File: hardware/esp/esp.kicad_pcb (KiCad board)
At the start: 2 copper layers, 100 x 80 mm, 89 parts, among them J1 Conn_01x02, J2 USB_C_Receptacle_USB2.0_16P, J3 USB_C_Receptacle_USB2.0_16P, J4 Conn_01x02, J5 Conn_Coaxial, J6 Conn_01x09_Pin, J7 Conn_01x06_Pin, J8 Conn_01x09_Pin, SW1 RESET, SW2 BOOT, U1 AMS1117-3.3, U2 CP2102N-Axx-xQFN20, U3 ESP32-S3-WROOM-1, U4 VL53L0X, U5 NRF24L01, U6 BME280, Y1 16MHz

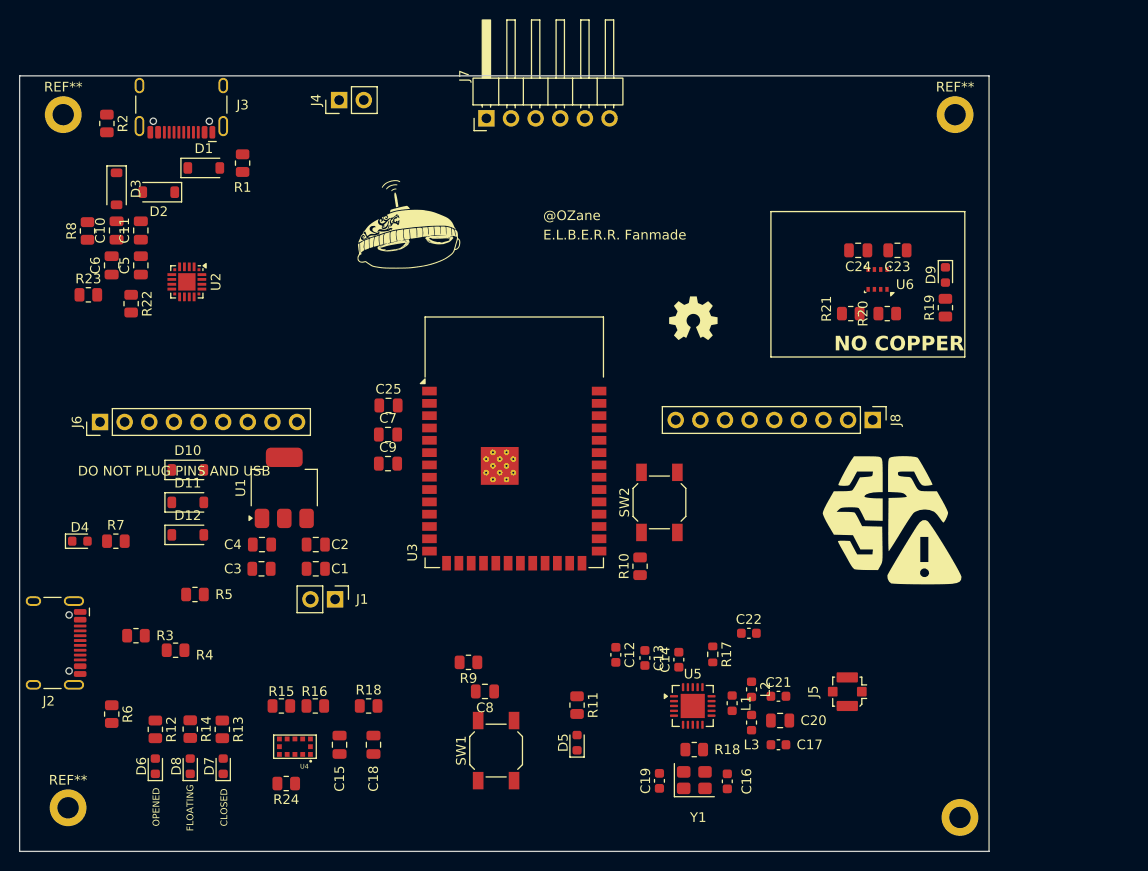
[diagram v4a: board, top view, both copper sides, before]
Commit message: Updating schematic, BOM, and component placement on PCB
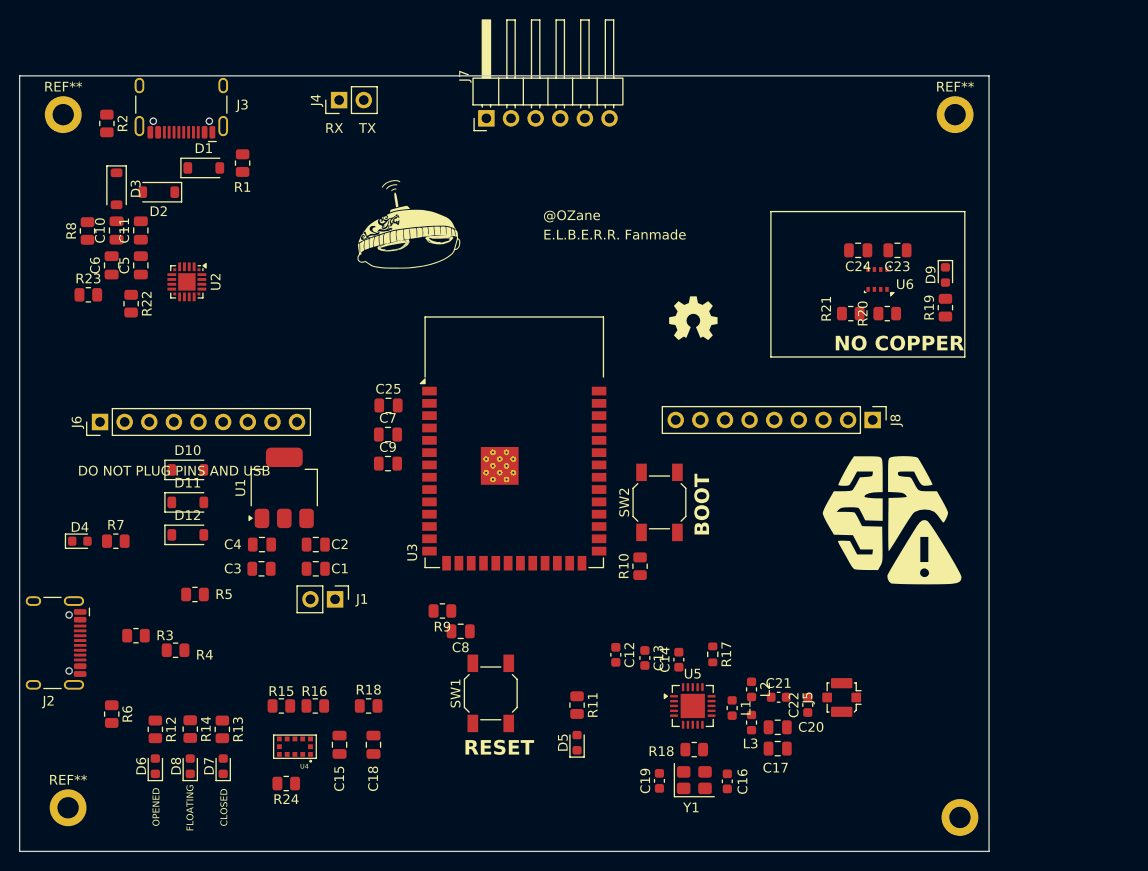
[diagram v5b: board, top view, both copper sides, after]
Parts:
- C17: footprint Capacitor_SMD:C_0603_1608Metric -> Capacitor_SMD:C_0805_2012Metric
- moved C22 9.57 mm to (166.3, 134.9), turned to 90 degrees
- moved C8 6.69 mm to (130.5, 127.3)
- moved R9 5.94 mm to (128.6, 125.2)
- moved SW1 5.93 mm to (133.6, 133.7)
- moved J5 0.83 mm to (169.8, 134.1)
- moved C20 0.74 mm to (163.2, 137.2)
- moved L1 0.50 mm to (158.5, 135.2)
- moved C17 0.41 mm to (163.2, 139.4)
- moved C21 0.10 mm to (163.3, 134.1)
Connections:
- C24 pad 1: +3V3 -> GND
- C24 pad 2: GND -> +3V3
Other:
- board text added: "BOOT"
- board text added: "RESET"

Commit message: Updating PCB
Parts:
- removed the R18 at (121.0, 135.0)
- moved D10 20.8 mm to (98.0, 131.0), turned to -90 degrees
- moved D11 12.8 mm to (98.0, 126.0), turned to 90 degrees
- moved D12 9.94 mm to (94.0, 122.8), turned to 90 degrees
- moved C12 8.70 mm to (155.2, 129.5), turned to 180 degrees
- moved C13 5.82 mm to (155.2, 131.2), turned to 180 degrees
- moved R4 5.49 mm to (106.6, 129.2)
- moved R3 5.49 mm to (102.5, 127.7)
- moved C6 3.01 mm to (97.5, 89.6)
- moved C10 2.50 mm to (97.5, 85.9)
- moved C11 2.50 mm to (95.0, 85.9)
- moved C5 2.50 mm to (95.0, 89.6)
- moved R17 1.49 mm to (157.8, 130.4)
- moved L2 1.04 mm to (161.0, 134.2), turned to 0 degrees
- moved C21 1.00 mm to (164.3, 134.2)
- moved C22 1.00 mm to (167.3, 135.0)
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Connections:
- U5 pad 21: (no net) -> GND
- U5 pad 3: SPI_SCK -> SCK
- U5 pad 4: SPI_MOSI -> MOSI
- U5 pad 5: SPI_MISO -> MISO
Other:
- board text removed: "NO COPPER"

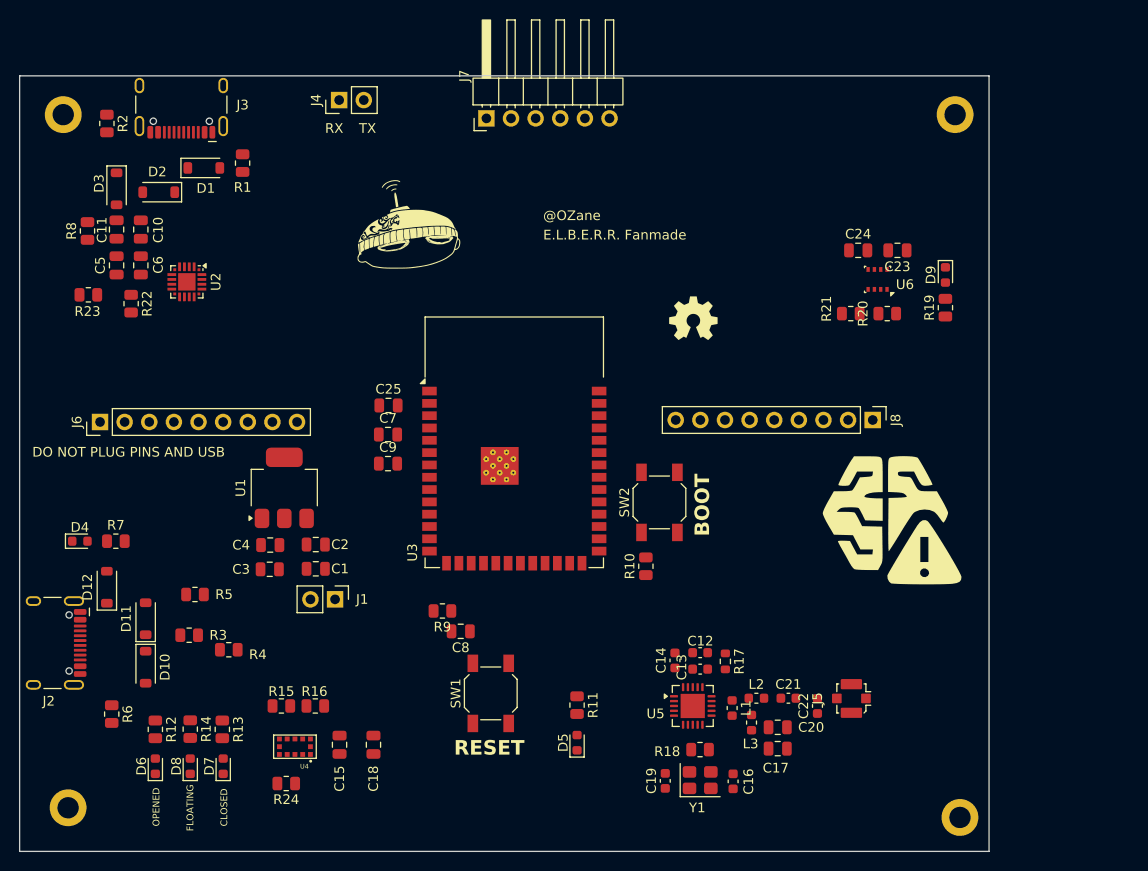
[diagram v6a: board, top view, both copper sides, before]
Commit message: Starting PCB routing, updating schematic pins and firmware pins for optimal routing
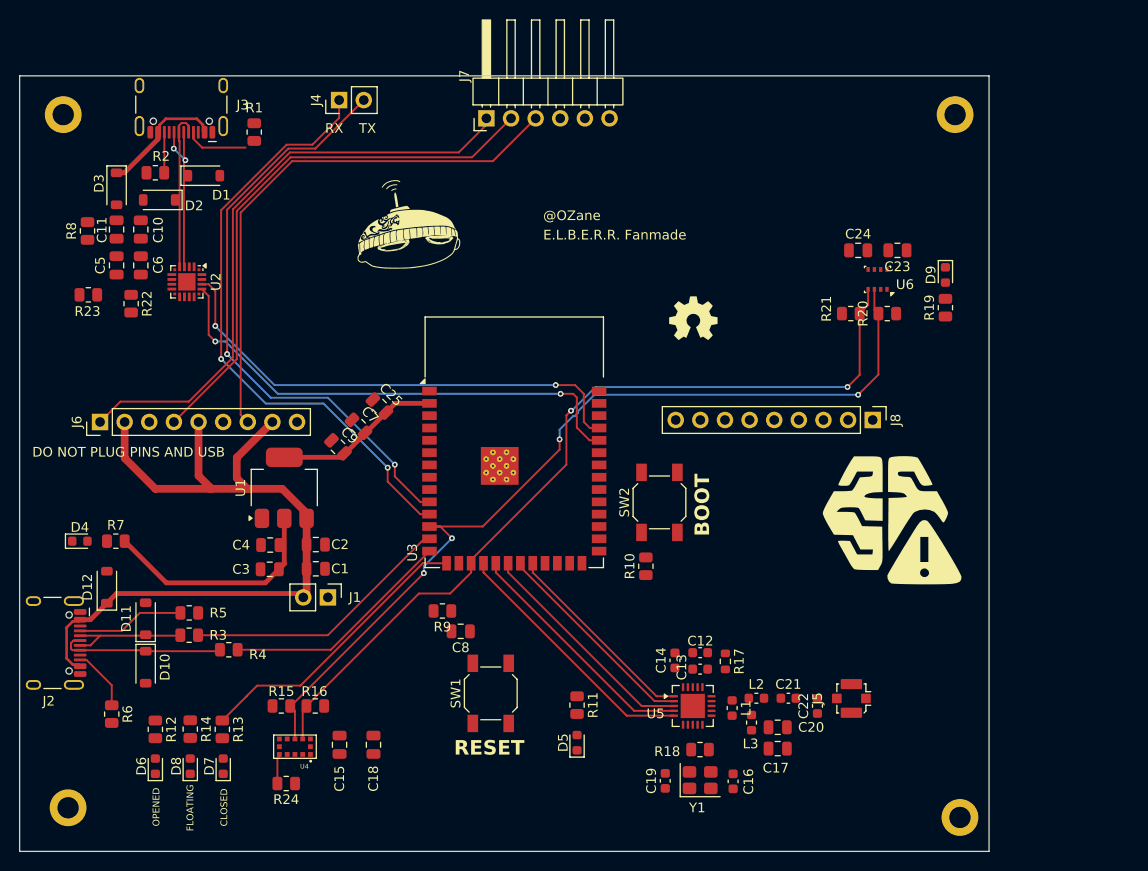
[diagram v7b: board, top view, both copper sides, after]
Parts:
- moved R2 7.13 mm to (99.0, 80.0), turned to 180 degrees
- moved C9 5.44 mm to (117.8, 108.3), turned to -45 degrees
- moved R1 3.42 mm to (109.2, 75.8), turned to 90 degrees
- moved C7 3.16 mm to (120.0, 106.1), turned to -45 degrees
- moved R5 1.99 mm to (102.5, 125.4)
- moved C25 0.94 mm to (122.1, 104.1), turned to -45 degrees
- moved D2 0.80 mm to (99.4, 82.8)
- moved D1 0.80 mm to (104.0, 80.3)
- moved J1 0.77 mm to (116.8, 123.8)
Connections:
- J7 pad 1: LP -> LH
- J7 pad 3: LH -> LP
- J7 pad 4: RH -> RP
- J7 pad 6: RP -> RH
- U3 pad 18: NRF_CSN -> unconnected-(U3-IO10-Pad18)
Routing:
- net SDA: track 0.00 -> 93.7 mm, vias 0 -> 4
- net SCL: track 0.00 -> 87.7 mm, vias 0 -> 2
- net +5V: track 0.00 -> 80.9 mm
- net RX2: track 0.00 -> 62.3 mm, vias 0 -> 2
- net LH: track 0.00 -> 62.2 mm
- net TX2: track 0.00 -> 61.6 mm, vias 0 -> 2
- net LV: track 0.00 -> 56.7 mm
- net LP: track 0.00 -> 56.4 mm
- net TX: track 0.00 -> 51.6 mm, vias 0 -> 2
- net RX: track 0.00 -> 50.9 mm, vias 0 -> 2
- net +3V3: track 0.00 -> 41.0 mm
- net C.SKULL: track 0.00 -> 29.9 mm
- net D-: track 0.00 -> 28.0 mm
- net MISO: track 0.00 -> 26.7 mm
- net MOSI: track 0.00 -> 25.2 mm
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
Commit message: Finishing PCB routing (PRE-DRC)
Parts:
- J7: footprint Connector_PinHeader_2.54mm:PinHeader_1x06_P2.54mm_Horizontal -> Connector_PinHeader_2.54mm:PinHeader_1x06_P2.54mm_Vertical
- moved C3 13.8 mm to (120.0, 110.6), turned to -90 degrees
- moved C4 10.3 mm to (117.5, 110.5), turned to -90 degrees
- moved D4 10.1 mm to (101.3, 118.0)
- moved R7 10.1 mm to (105.0, 118.0)
- moved C9 5.19 mm to (118.7, 103.1), turned to -90 degrees
- moved C7 3.42 mm to (121.5, 103.1), turned to -90 degrees
- moved C25 2.48 mm to (124.4, 103.1), turned to -90 degrees
- moved C24 1.45 mm to (172.5, 86.9), turned to -90 degrees
- moved C23 1.01 mm to (175.7, 87.0), turned to -90 degrees
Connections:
- net LP renamed LE
- net RP renamed RE
- C5 pad 1: Net-(D3-A1) -> +5V
- C6 pad 1: Net-(D3-A1) -> +5V
- D3 pad 1: Net-(D3-A1) -> +5V
- J3 pad A4: Net-(D3-A1) -> +5V
- J3 pad A9: Net-(D3-A1) -> +5V
- J3 pad B4: Net-(D3-A1) -> +5V
- J3 pad B9: Net-(D3-A1) -> +5V
- R23 pad 1: Net-(D3-A1) -> +5V
- U2 pad 7: Net-(D3-A1) -> +5V
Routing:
- net +3V3: track 41.0 -> 298.5 mm, vias 0 -> 8
- net +5V: track 80.9 -> 231.8 mm, vias 0 -> 2
- net O.SKULL: track 0.00 -> 72.7 mm, vias 0 -> 2
- net TEMP_LED: track 0.00 -> 66.9 mm, vias 0 -> 2
- net RE: track 0.00 -> 54.1 mm
- net RH: track 0.00 -> 50.1 mm
- net RV: track 0.00 -> 49.1 mm
- net NF.SKULL: track 0.00 -> 45.3 mm, vias 0 -> 2
- net EN: track 0.00 -> 39.6 mm, vias 0 -> 2
- net NRFLED: track 0.00 -> 34.0 mm, vias 0 -> 2
- net Net-(U2-~{RST}): track 0.00 -> 17.7 mm, vias 0 -> 2
- net BOOT: track 0.00 -> 14.1 mm
- net Net-(D3-A1): track 13.1 -> 0.00 mm
- net /VDD: track 0.00 -> 10.3 mm
- net Net-(U5-XC2): track 0.00 -> 9.65 mm
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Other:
- board text added: "H = Horizontal V = Vertical E = Eyelid R = Right L = Left"
- board text added: "LE"
- board text added: "LH"
- board text added: "LV"
- board text added: "RE"
- board text added: "RH"
- board text added: "RV"
